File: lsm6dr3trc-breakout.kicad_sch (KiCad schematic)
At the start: 13 parts, among them CN1 AFC10-S04QCA-00, CN2 AFC10-S04QCA-00, J1 Conn_01x06_Pin, J2 Conn_01x04_Pin, U1 LSM6DS3TR-C

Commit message: fix qwiic pinout, redo footprint
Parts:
- added H1, H2: MountingHole, MountingHole:MountingHole_2.2mm_M2, symbol Mechanical:MountingHole
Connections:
- net GND: now also CN1.1, CN1.5, CN1.6, CN2.1, CN2.5, CN2.6; no longer CN1.4, CN2.4
- net SCL: now also CN1.4, CN2.4; no longer CN1.1, CN2.1
- net SDA: now also CN1.3, CN2.3; no longer CN1.2, CN2.2
- net VDD: now also CN1.2, CN2.2; no longer CN1.3, CN2.3
- no-connect marks 4 -> 0

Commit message: unified IMU footprint
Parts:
- CN1, CN2: footprint lsm6dr3trc-breakout:CONN-SMD_AFC10-S04QCA-00 -> qwiic:CONN-SMD_AFC10-S04QCA-00
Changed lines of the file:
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@@
 			)
 		)
-		(property "Footprint" "lsm6dr3trc-breakout:CONN-SMD_AFC10-S04QCA-00"
+		(property "Footprint" "qwiic:CONN-SMD_AFC10-S04QCA-00"
 			(at 189.23 88.9 0)
 			(effects
@@
 			)
 		)
-		(property "Footprint" "lsm6dr3trc-breakout:CONN-SMD_AFC10-S04QCA-00"
+		(property "Footprint" "qwiic:CONN-SMD_AFC10-S04QCA-00"
 			(at 189.23 63.5 0)
 			(effects

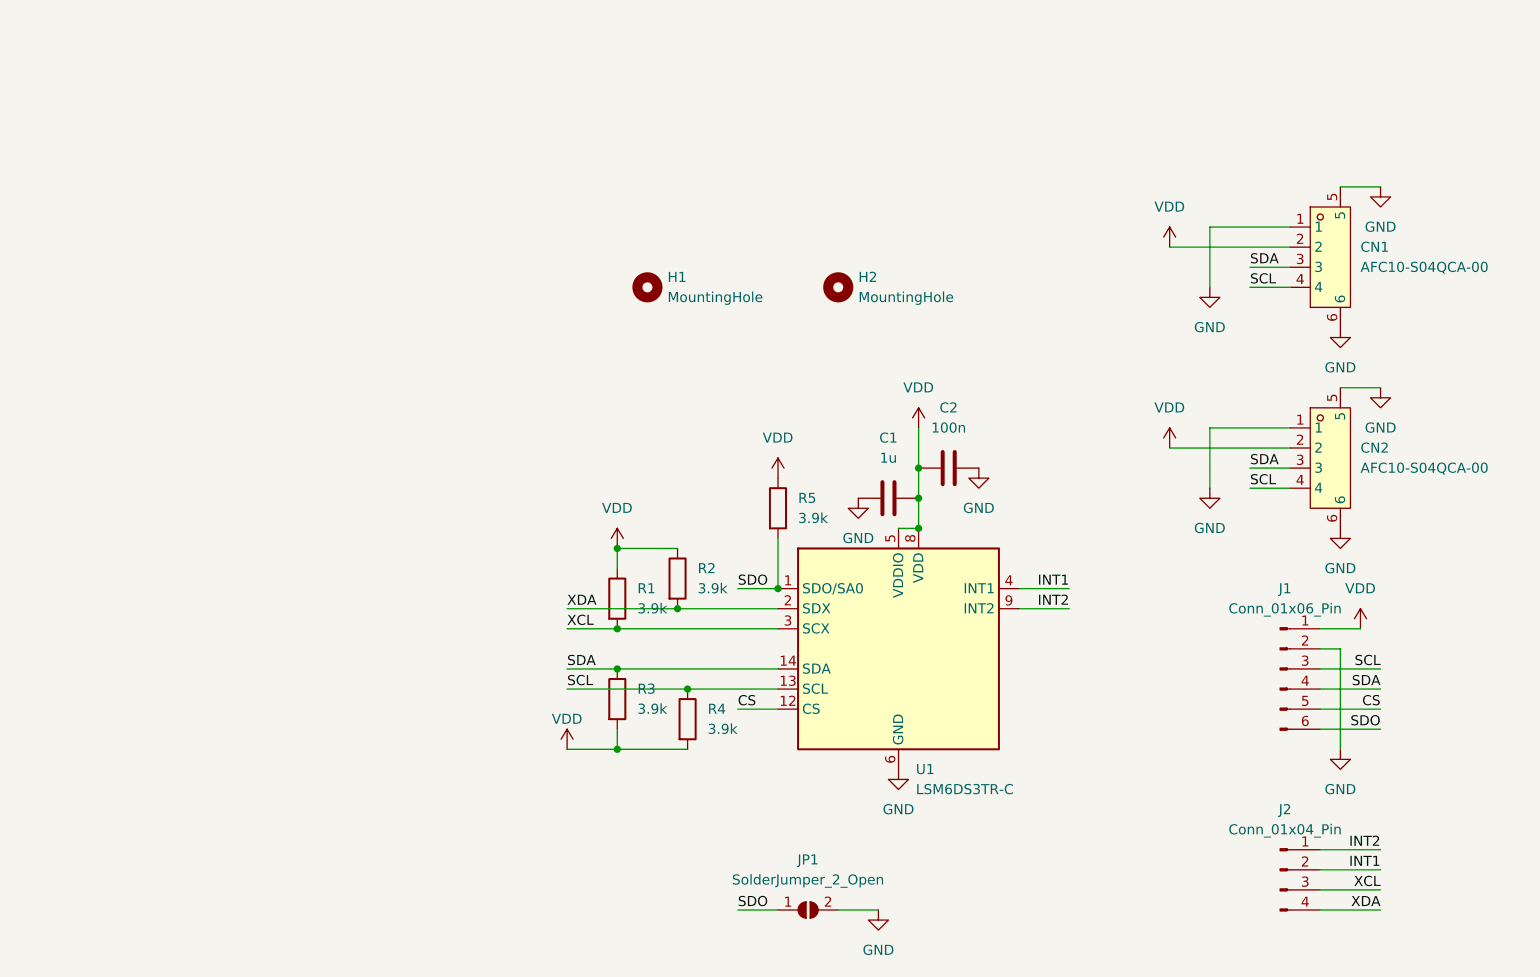
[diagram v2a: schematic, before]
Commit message: fix csb resistor, beautify schematic
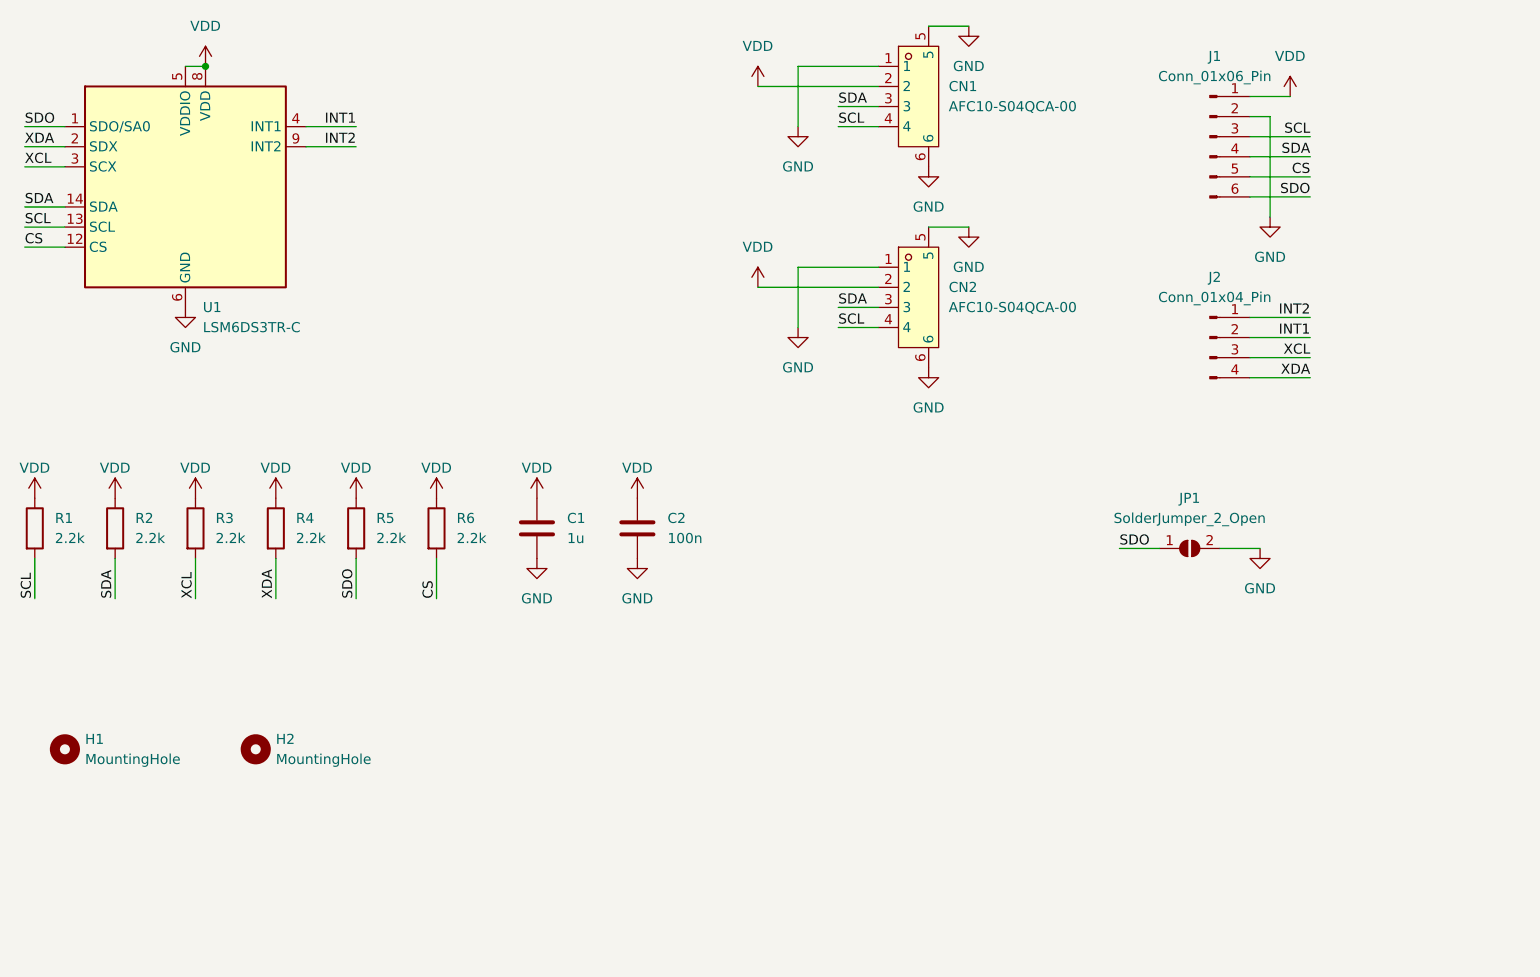
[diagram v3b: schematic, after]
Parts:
- added R6: 2.2k, Resistor_SMD:R_0402_1005Metric, symbol Device:R
- R1, R2, R3, R4, R5: value 3.9k -> 2.2k
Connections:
- net CS: now also R6.2
- net GND: now also C1.2; no longer C1.1
- net SCL: now also R1.2; no longer R4.1
- net SDA: now also R2.2; no longer R3.1
- net VDD: now also C1.1, R3.1, R4.1, R6.1; no longer C1.2, R3.2, R4.2
- net XCL: now also R3.2; no longer R1.2
- net XDA: now also R4.2; no longer R2.2
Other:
- moved on the sheet: CN1, CN2, H1, H2, J1, J2, JP1, U1

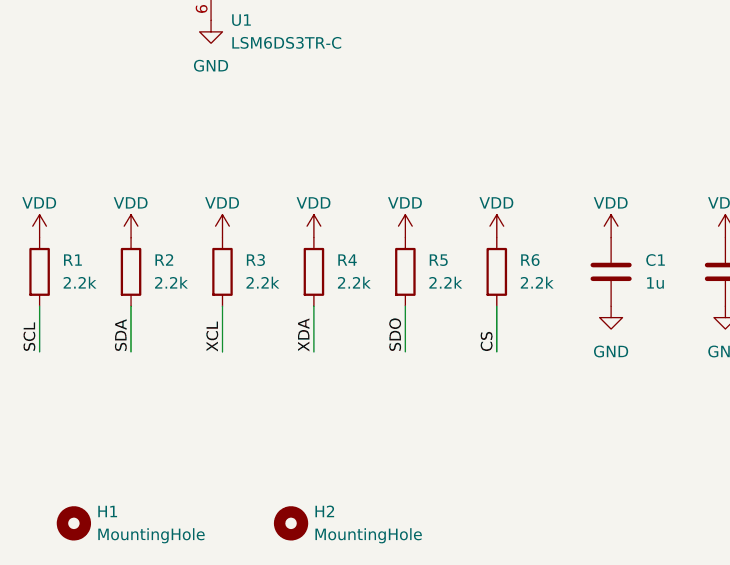
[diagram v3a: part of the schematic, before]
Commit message: use lower pullups
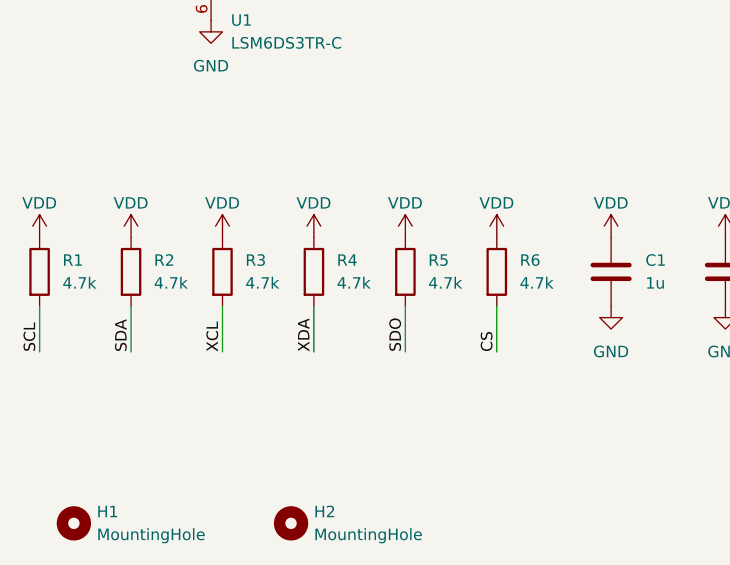
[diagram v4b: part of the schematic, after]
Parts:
- R1, R2, R3, R4, R5, R6: value 2.2k -> 4.7k
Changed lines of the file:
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@@
 			)
 		)
-		(property "Value" "2.2k"
+		(property "Value" "4.7k"
 			(at 68.58 82.5499 0)
 			(effects
@@
 			)
 		)
-		(property "Value" "2.2k"
+		(property "Value" "4.7k"
 			(at 48.26 82.5499 0)
 			(effects
@@
 			)
 		)
-		(property "Value" "2.2k"
+		(property "Value" "4.7k"
 			(at 58.42 82.5499 0)
 			(effects
@@
 			)
 		)
-		(property "Value" "2.2k"
+		(property "Value" "4.7k"
 			(at 27.94 82.5499 0)
 			(effects
@@
 			)
 		)
-		(property "Value" "2.2k"
+		(property "Value" "4.7k"
 			(at 38.1 82.5499 0)
 			(effects
@@
 			)
 		)
-		(property "Value" "2.2k"
+		(property "Value" "4.7k"
 			(at 78.74 82.5499 0)
 			(effects
